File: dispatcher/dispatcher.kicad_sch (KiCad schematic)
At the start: 30 parts, among them J1 Conn_01x06_Female, J2 Conn_01x18, K1 HFD2_005-S-L2-D, K2 HFD2_005-S-L2-D, U1 INA3221_Module, U2 ULN2803A, U3 ULN2803A, U5 MCP2551-I-P, U6 ChinaBluePill-bluepill-D3_Boa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

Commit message: mainboard4 ready for production
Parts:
- gave numbers to parts that had none: 1
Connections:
- net RELAY0_0 is gone; now on net RELAY_SET0: U6.30 (PA5)
- net RELAY0_1 is gone; now on net RELAY_SET1: U6.31 (PA6)
- net RELAY1_0 is gone; now on net RELAY_SET2: U6.32 (PA7)
- net +12V: now also U3.10 (COM); no longer U2.10 (COM)
- net +5V: now also U2.10 (COM); no longer U3.10 (COM)
- net GND: no longer U2.9 (GND)
- net LED0: now also U2.5 (I5), U6.8 (PA11); no longer U3.1 (I1), U6.3 (PB14)
- net LED1: now also U2.6 (I6), U6.9 (PA12); no longer U3.2 (I2), U6.4 (PB15)
- net LED2: now also U2.7 (I7); no longer U3.3 (I3)
- net LED3: now also U2.8 (I8); no longer U3.4 (I4), U6.8 (PA11)
- net RELAY0: now also U6.29 (PA4)
- net TURN1A: now also U3.1 (I1); no longer U2.5 (I5)
- net TURN1B: now also U3.2 (I2); no longer U2.6 (I6)
- net TURN2A: now also U3.3 (I3); no longer U2.7 (I7)
- net TURN2B: now also U3.4 (I4); no longer U2.8 (I8)
- net at U3.13 (O6): no longer J_LED_2.4 (Pin_4)
- net at U3.14 (O5): no longer J_LED_2.2 (Pin_2)
- net at U3.15 (O4): no longer J_LED_1.8 (Pin_8)
- net at U3.16 (O3): no longer J_LED_1.6 (Pin_6)
- net at U3.17 (O2): no longer J_LED_1.4 (Pin_4)
- net at U3.18 (O1): no longer J_LED_1.2 (Pin_2)
- net LED4 renamed TURN3A
- net TURN3A: now also U6.3 (PB14); no longer U6.9 (PA12)
- net LED5: no longer names the net of U6.12 (PB4)
- net LED5: no longer U3.6 (I6)
- net RELAY1_1: no longer names the net of U6.33 (PB0)
- new net TURN3B: U3.6 (I6), U6.4 (PB15)
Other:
- moved on the sheet: J2, J_LED_1, J_LED_2, R1, R2, R3, R4, R5, R6, U3

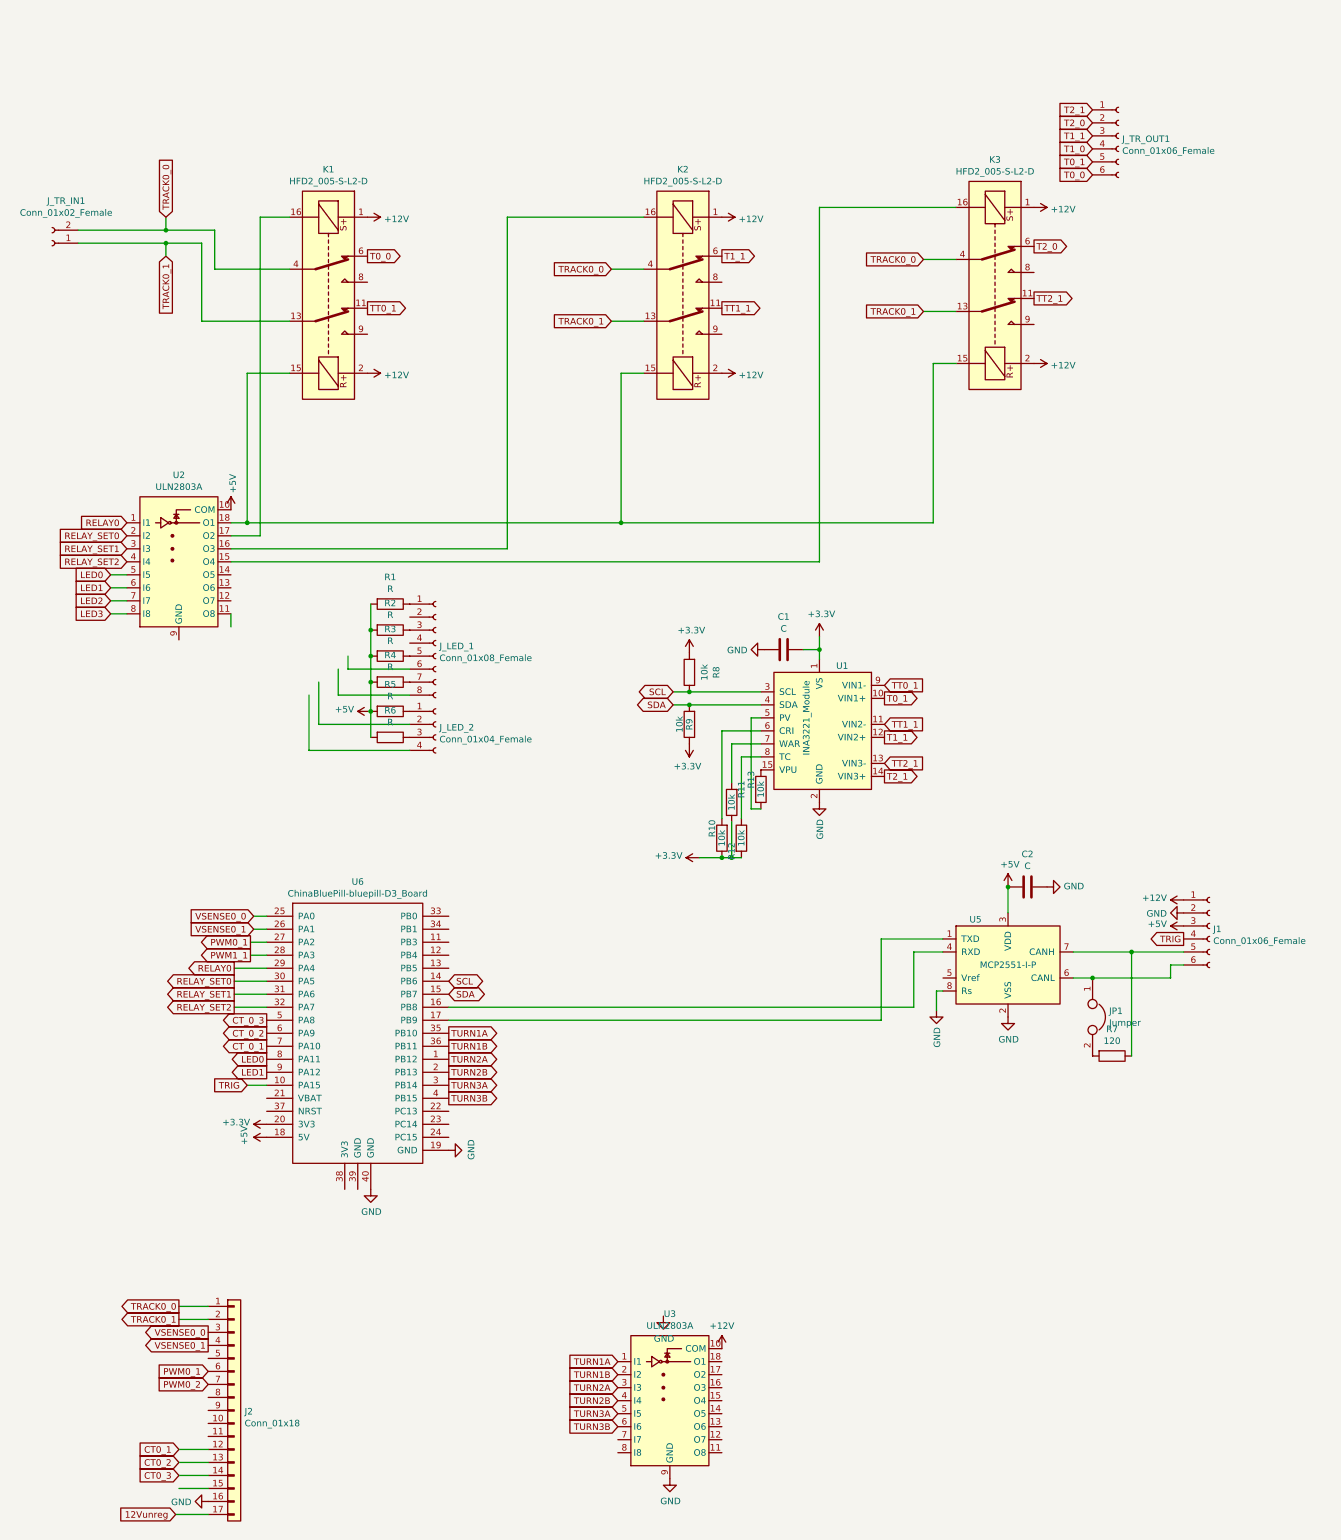
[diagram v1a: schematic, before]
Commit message: updated dispatcher
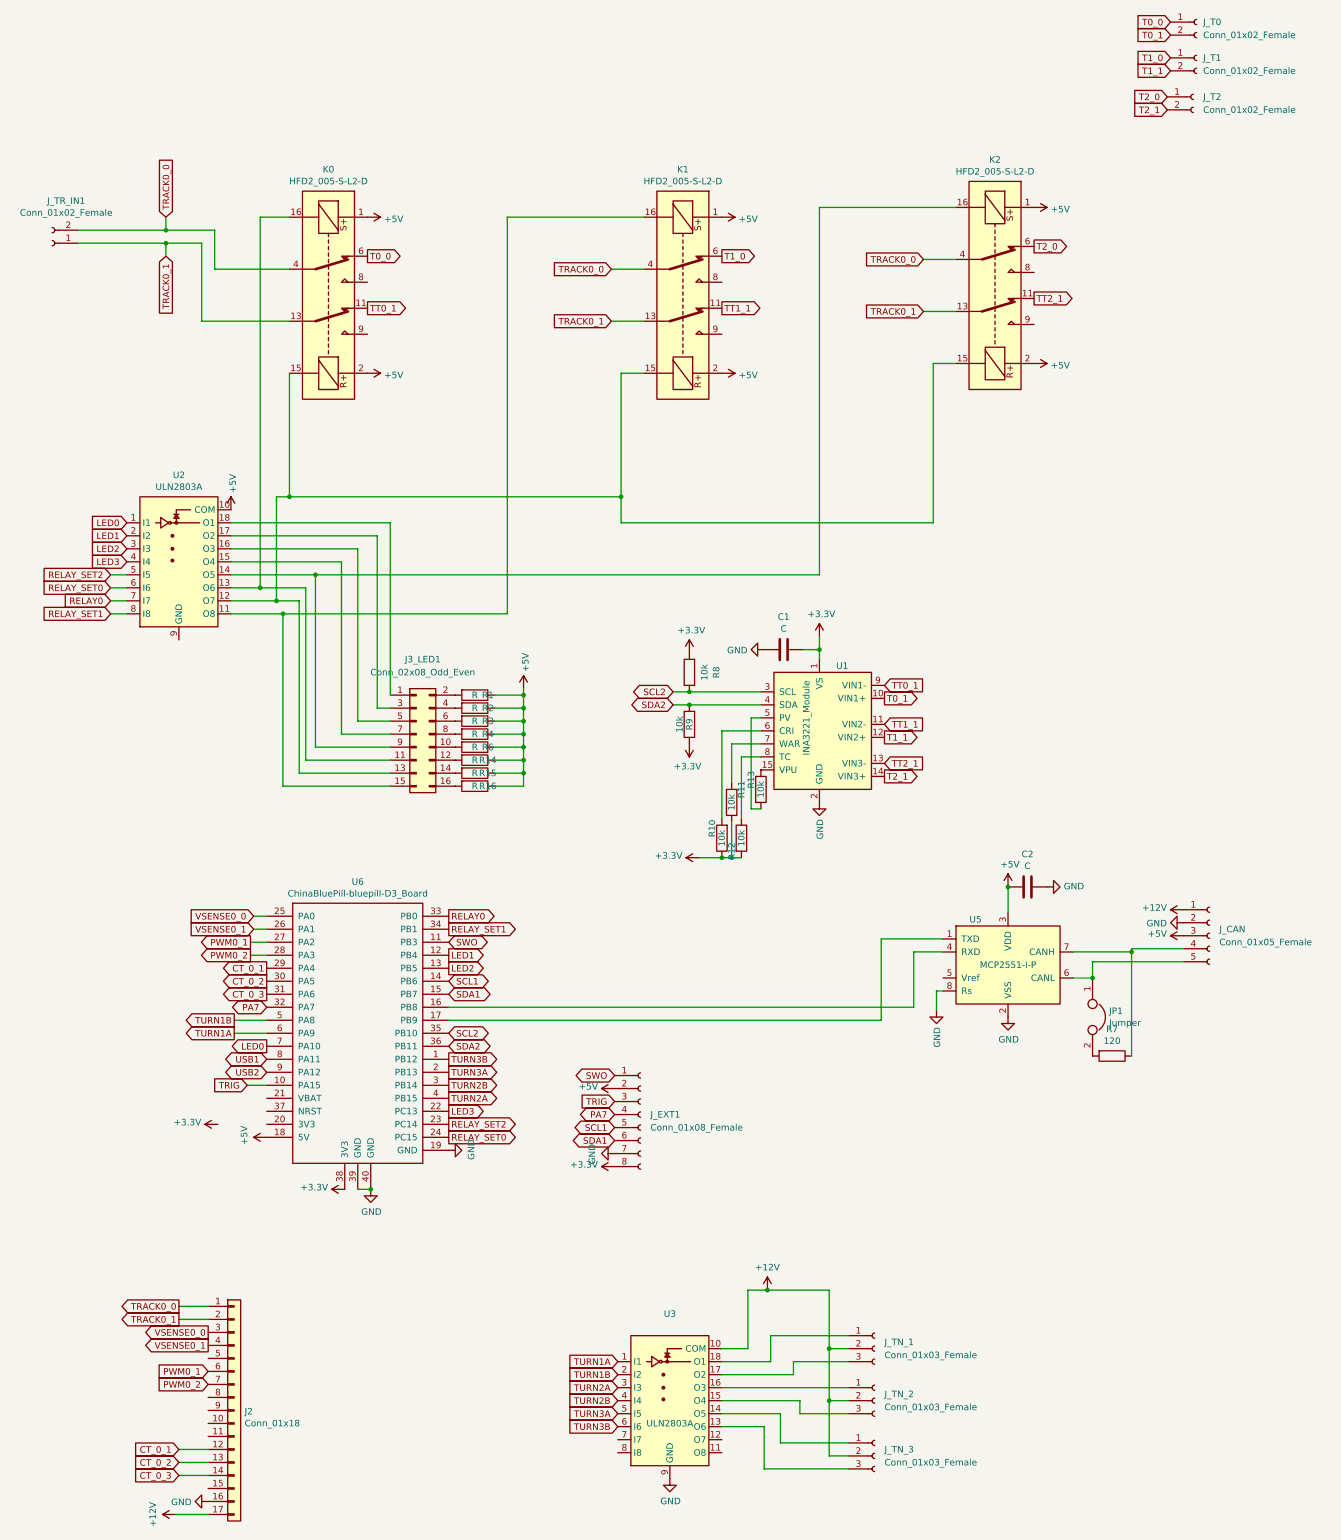
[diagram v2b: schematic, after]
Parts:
- removed J1, J_TR_OUT1: Conn_01x06_Female, Connector_PinHeader_2.54mm:PinHeader_1x06_P2.54mm_Vertical, symbol Connector:Conn_01x06_Female
- removed J_LED_1: Conn_01x08_Female, Connector_PinHeader_2.54mm:PinHeader_1x08_P2.54mm_Vertical, symbol Connector:Conn_01x08_Female
- removed J_LED_2: Conn_01x04_Female, Connector_PinHeader_2.54mm:PinHeader_1x04_P2.54mm_Vertical, symbol Connector:Conn_01x04_Female
- removed R5: R, Resistor_THT:R_Axial_DIN0207_L6.3mm_D2.5mm_P7.62mm_Horizontal, symbol Device:R
- added J3_LED1: Conn_02x08_Odd_Even, Connector_PinHeader_2.54mm:PinHeader_2x08_P2.54mm_Vertical, symbol Connector_Generic:Conn_02x08_Odd_Even
- added J_CAN: Conn_01x05_Female, Connector_PinHeader_2.54mm:PinHeader_1x05_P2.54mm_Vertical, symbol Connector:Conn_01x05_Female
- added J_EXT1: Conn_01x08_Female, Connector_PinHeader_2.54mm:PinHeader_1x08_P2.54mm_Vertical, symbol Connector:Conn_01x08_Female
- added J_T0, J_T1, J_T2: Conn_01x02_Female, Connector_PinHeader_2.54mm:PinHeader_1x02_P2.54mm_Vertical, symbol Connector:Conn_01x02_Female
- added J_TN_1, J_TN_2, J_TN_3: Conn_01x03_Female, Connector_PinHeader_2.54mm:PinHeader_1x03_P2.54mm_Vertical, symbol Connector:Conn_01x03_Female
- added R14, R15, R16: R, Resistor_THT:R_Axial_DIN0207_L6.3mm_D2.5mm_P7.62mm_Horizontal, symbol Device:R
- renumbered K1 to K0, K2 to K1, K3 to K2
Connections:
- net 12Vunreg is gone; now on net +12V: J2.17 (Pin_17)
- net CT0_1 is gone; now on net CT_0_1: J2.12 (Pin_12)
- net CT0_2 is gone; now on net CT_0_2: J2.13 (Pin_13)
- net CT0_3 is gone; now on net CT_0_3: J2.14 (Pin_14)
- net PWM1_1 is gone; now on net PWM0_2: U6.28 (PA3)
- net +12V: now also J_CAN.1 (Pin_1), J_TN_1.2 (Pin_2), J_TN_2.2 (Pin_2), J_TN_3.2 (Pin_2); no longer K0.1, K0.2, K1.1, K1.2, K2.1, K2.2
- net +3V3: now also U6.38 (3V3), J_EXT1.8 (Pin_8); no longer U6.20 (3V3)
- net +5V: now also K0.1, K0.2, K1.1, K1.2, K2.1, K2.2, R1.1, R2.1, R3.1, R4.1, R6.1, J_CAN.3 (Pin_3), J_EXT1.2 (Pin_2), R14.1, R15.1, R16.1; no longer R1.2, R2.2, R3.2, R4.2, R6.2
- net CT_0_1: now also U6.29 (PA4); no longer U6.7 (PA10)
- net CT_0_2: now also U6.30 (PA5); no longer U6.6 (PA9)
- net CT_0_3: now also U6.31 (PA6); no longer U6.5 (PA8)
- net GND: now also U6.39 (GND), J_CAN.2 (Pin_2), J_EXT1.7 (Pin_7)
- net LED0: now also U2.1 (I1), U6.7 (PA10); no longer U2.5 (I5), U6.8 (PA11)
- net LED1: now also U2.2 (I2), U6.12 (PB4); no longer U2.6 (I6), U6.9 (PA12)
- net LED2: now also U2.3 (I3), U6.13 (PB5); no longer U2.7 (I7)
- net LED3: now also U2.4 (I4), U6.22 (PC13); no longer U2.8 (I8)
- net RELAY0: now also U2.7 (I7), U6.33 (PB0); no longer U2.1 (I1), U6.29 (PA4)
- net RELAY_SET0: now also U2.6 (I6), U6.24 (PC15); no longer U2.2 (I2), U6.30 (PA5)
- net RELAY_SET1: now also U2.8 (I8), U6.34 (PB1); no longer U2.3 (I3), U6.31 (PA6)
- net RELAY_SET2: now also U2.5 (I5), U6.23 (PC14); no longer U2.4 (I4), U6.32 (PA7)
- net T0_0: now also J_T0.1 (Pin_1)
- net T0_1: now also J_T0.2 (Pin_2)
- net T1_0: now also K1.6, J_T1.1 (Pin_1)
- net T1_1: now also J_T1.2 (Pin_2); no longer K1.6
- net T2_0: now also J_T2.1 (Pin_1)
- net T2_1: now also J_T2.2 (Pin_2)
- net TRIG: now also J_EXT1.3 (Pin_3)
- net TURN1A: now also U6.6 (PA9); no longer U6.35 (PB10)
- net TURN1B: now also U6.5 (PA8); no longer U6.36 (PB11)
- net TURN2A: now also U6.4 (PB15); no longer U6.1 (PB12)
- net TURN2B: now also U6.3 (PB14); no longer U6.2 (PB13)
- net TURN3A: now also U6.2 (PB13); no longer U6.3 (PB14)
- net TURN3B: now also U6.1 (PB12); no longer U6.4 (PB15)
- net at JP1.1, U5.6 (CANL): now also J_CAN.5 (Pin_5)
- net at R7.1, U5.7 (CANH): now also J_CAN.4 (Pin_4)
- net SWO: now reaches U6.11 (PB3)
- net SWO: now also J_EXT1.1 (Pin_1)
- net at U2.11 (O8): now also K1.16, J3_LED1.15 (Pin_15)
- net at U2.12 (O7): now also K0.15, K1.15, K2.15, J3_LED1.13 (Pin_13)
- net at U2.13 (O6): now also K0.16, J3_LED1.11 (Pin_11)
- net at U2.14 (O5): now also K2.16, J3_LED1.9 (Pin_9)
- net at U2.15 (O4): now also J3_LED1.7 (Pin_7); no longer K2.16
- net at U2.16 (O3): now also J3_LED1.5 (Pin_5); no longer K1.16
- net at U2.17 (O2): now also J3_LED1.3 (Pin_3); no longer K0.16
- net at U3.13 (O6): now also J_TN_3.3 (Pin_3)
- net at U3.14 (O5): now also J_TN_3.1 (Pin_1)
- net at U3.15 (O4): now also J_TN_2.3 (Pin_3)
- net at U3.16 (O3): now also J_TN_2.1 (Pin_1)
- net at U3.17 (O2): now also J_TN_1.3 (Pin_3)
- net at U3.18 (O1): now also J_TN_1.1 (Pin_1)
- net SCL renamed SCL2
- net SCL2: now also U6.35 (PB10); no longer U6.14 (PB6)
- net SDA renamed SDA2
- net SDA2: now also U6.36 (PB11); no longer U6.15 (PB7)
- new net: J3_LED1.1 (Pin_1), U2.18 (O1)
- new net: J3_LED1.10 (Pin_10), R6.2
- new net: J3_LED1.12 (Pin_12), R14.2
- new net: J3_LED1.14 (Pin_14), R15.2
- new net: J3_LED1.16 (Pin_16), R16.2
- new net: J3_LED1.2 (Pin_2), R1.2
- new net: J3_LED1.4 (Pin_4), R2.2
- new net: J3_LED1.6 (Pin_6), R3.2
- new net: J3_LED1.8 (Pin_8), R4.2
- new net PA7: J_EXT1.4 (Pin_4), U6.32 (PA7)
- new net SCL1: J_EXT1.5 (Pin_5), U6.14 (PB6)
- new net SDA1: J_EXT1.6 (Pin_6), U6.15 (PB7)
- new net USB1: U6.8 (PA11)
- new net USB2: U6.9 (PA12)

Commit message: ..
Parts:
- renumbered J_CAN to J_CAN1
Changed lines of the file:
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@@
   (symbol (lib_id "Connector:Conn_01x05_Female") (at 269.24 198.12 0) (unit 1)
     (in_bom yes) (on_board yes) (fields_autoplaced)
-    (property "Reference" "J_CAN" (id 0) (at 271.145 196.8499 0)
+    (property "Reference" "J_CAN1" (id 0) (at 271.145 196.8499 0)
       (effects (font (size 1.27 1.27)) (justify left))
     )
@@
     )
     (path "/5cb45bca-ea3d-4d76-b8ba-af00cf7d92dd"
-      (reference "J_CAN") (unit 1) (value "Conn_01x05_Female") (footprint "Connector_PinHeader_2.54mm:PinHeader_1x05_P2.54mm_Vertical")
+      (reference "J_CAN1") (unit 1) (value "Conn_01x05_Female") (footprint "Connector_PinHeader_2.54mm:PinHeader_1x05_P2.54mm_Vertical")
     )
     (path "/c359a0e9-b7f6-4a78-a5f8-2dae089c3c3f"
